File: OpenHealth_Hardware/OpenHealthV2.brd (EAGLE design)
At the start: 128.3 x 134.6 mm, 25 parts

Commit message: Reparacion de placa principal - modo demo
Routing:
- net GND: track 140.3 -> 0.00 mm
- net VIN: track 85.2 -> 0.00 mm
- net LCA_RED: track 79.8 -> 0.00 mm
- net LCA_BLK: track 72.2 -> 0.00 mm
- net LCA_WHT: track 64.6 -> 0.00 mm
- net D_SCL: track 63.2 -> 0.00 mm
- net D_SDA: track 62.1 -> 0.00 mm
- net D12: track 58.5 -> 0.00 mm
- net LCA_GRN: track 56.9 -> 0.00 mm
- net LCA_YLW: track 49.3 -> 0.00 mm
- net LCA_CLK: track 32.1 -> 0.00 mm
- net LCA_DAT: track 29.5 -> 0.00 mm
- net 3.3V: track 18.6 -> 0.00 mm
- net B2: track 11.1 -> 0.00 mm
- net B1: track 7.32 -> 0.00 mm
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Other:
- board size 128.3 x 134.6 mm -> 128.3 x 133.3 mm

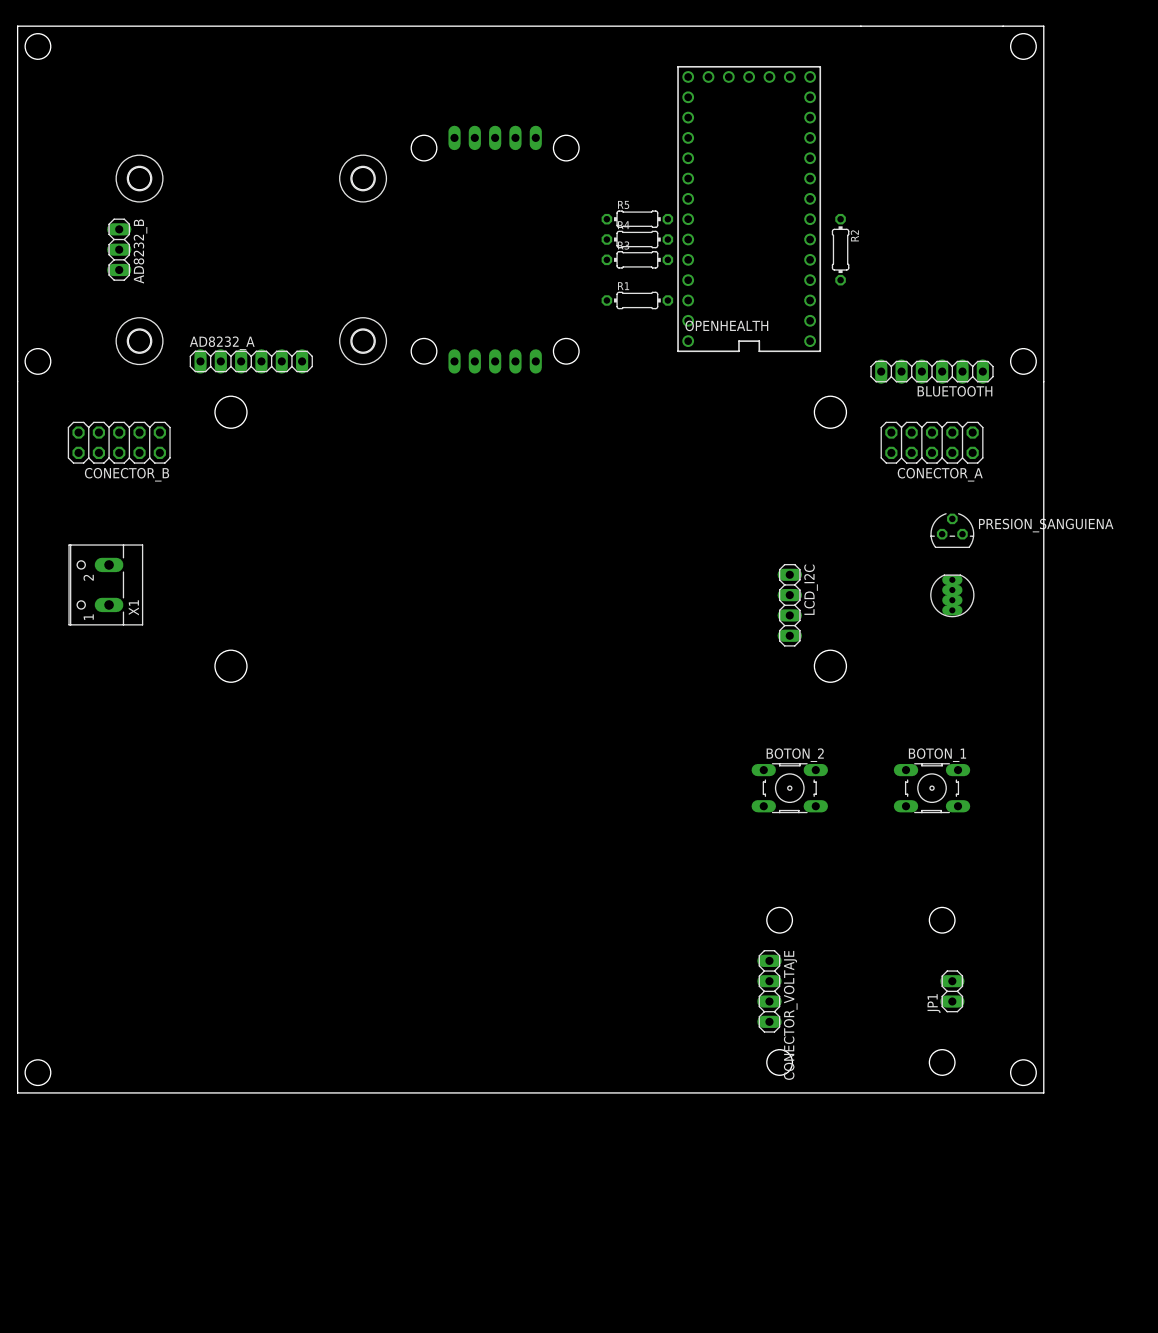
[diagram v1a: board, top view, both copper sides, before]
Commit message: Creacion de la Primera Libreria
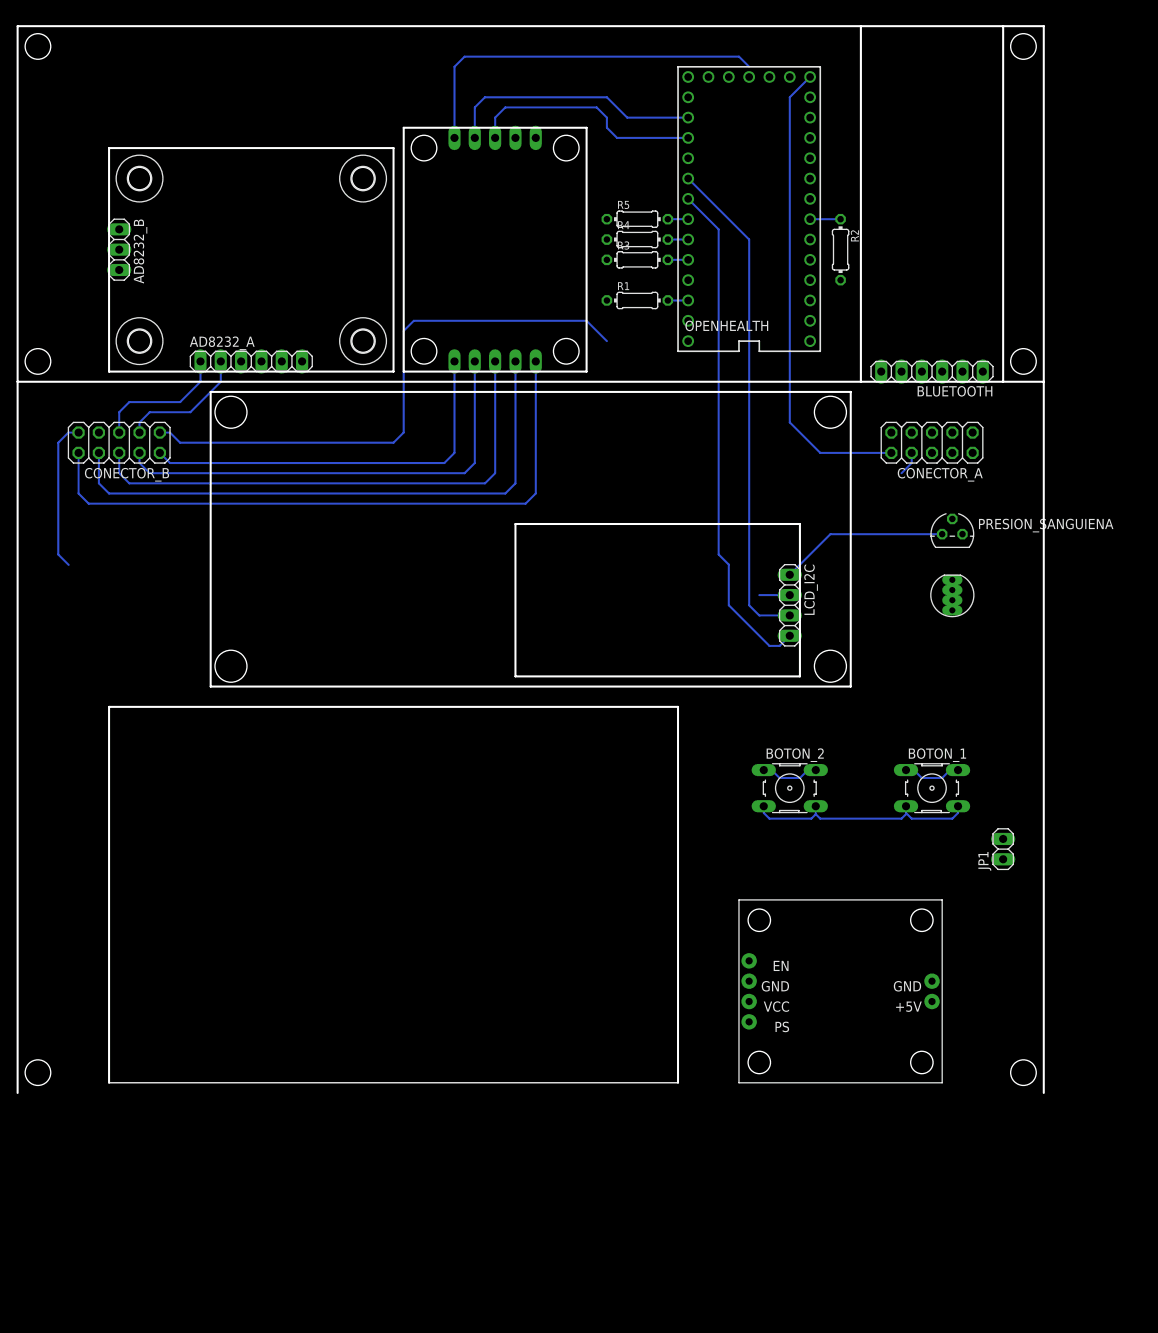
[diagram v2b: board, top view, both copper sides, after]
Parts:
- removed CONECTOR_VOLTAJE: (no value), pinhead:1X04
- removed X1: (no value), con-wago-500:W237-102
- added U$5: LIPOWER, Bateria:LIPOWER
- moved JP1 18.9 mm to (54.6, 50.8)
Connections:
- removed net N$1: CONECTOR_VOLTAJE.1, X1.1
- new net N$5: OPENHEALTH.VIN
- new net PIN_EN: JP1.1, U$5.PIN_EN
- net GND: now also JP1.2, U$5.PIN_GND1, U$5.PIN_GND2; no longer CONECTOR_VOLTAJE.2, X1.2
- net VIN: no longer CONECTOR_VOLTAJE.3, OPENHEALTH.VIN
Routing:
- net GND: track 0.00 -> 134.0 mm
- net LCA_RED: track 0.00 -> 79.8 mm
- net VIN: track 0.00 -> 75.0 mm
- net LCA_BLK: track 0.00 -> 72.2 mm
- net LCA_WHT: track 0.00 -> 64.6 mm
- net D_SCL: track 0.00 -> 63.2 mm
- net D_SDA: track 0.00 -> 62.1 mm
- net D12: track 0.00 -> 58.5 mm
- net LCA_GRN: track 0.00 -> 56.9 mm
- net LCA_YLW: track 0.00 -> 49.3 mm
- net LCA_CLK: track 0.00 -> 32.1 mm
- net LCA_DAT: track 0.00 -> 29.5 mm
- net 3.3V: track 0.00 -> 18.6 mm
- net B2: track 0.00 -> 11.1 mm
- net B1: track 0.00 -> 7.32 mm
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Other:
- outline, holes or cut-outs redrawn

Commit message: Creacion de los modulos de bluetooth y ad8232 asi como el cambio de nombre de la libreria y la utilizacion de la libreria en el proyecto
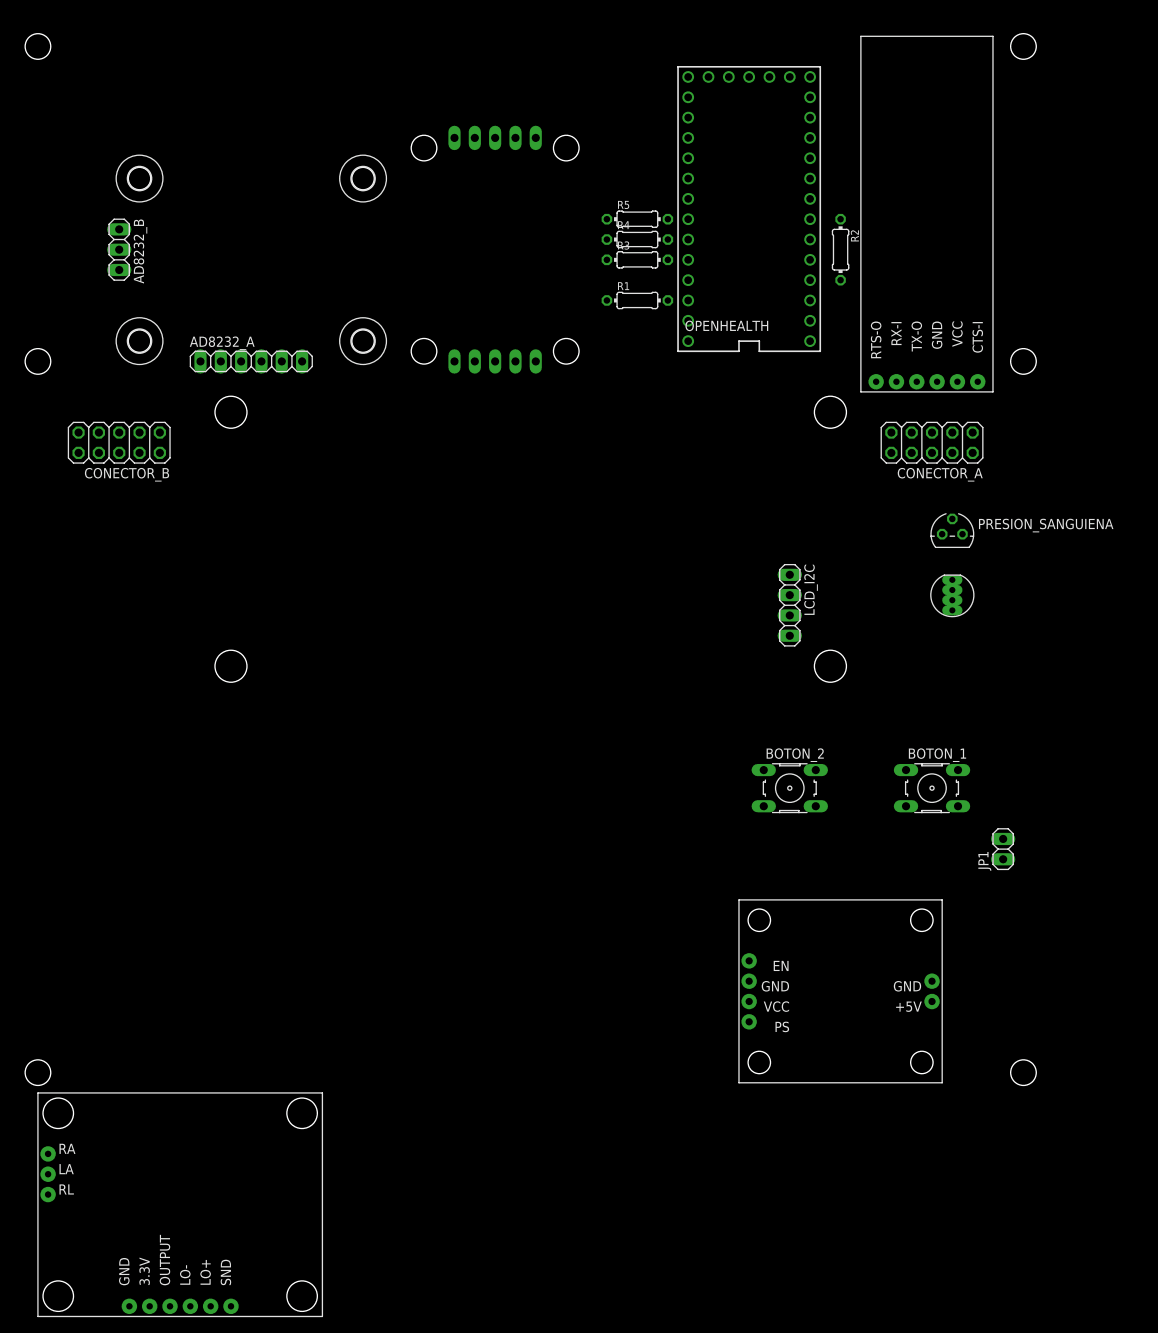
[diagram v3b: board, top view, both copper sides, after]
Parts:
- removed BLUETOOTH: (no value), pinhead:1X06
- added U$6: BLUETOOTH_HC05, OpenHealth:BLUETOOTH_HC05
- added U$7: AD8232, OpenHealth:AD8232
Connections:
- net BLUETOOTH_RX: now also U$6.PIN_RX-I; no longer BLUETOOTH.2
- net BLUETOOTH_TX: no longer BLUETOOTH.3
- net GND: now also U$6.PIN_GND; no longer BLUETOOTH.4
- net N$5: now also U$5.PIN_VCC
- net VIN: now also U$6.PIN_VCC; no longer BLUETOOTH.5
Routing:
- net GND: track 134.0 -> 0.00 mm
- net LCA_RED: track 79.8 -> 0.00 mm
- net VIN: track 75.0 -> 0.00 mm
- net LCA_BLK: track 72.2 -> 0.00 mm
- net LCA_WHT: track 64.6 -> 0.00 mm
- net D_SCL: track 63.2 -> 0.00 mm
- net D_SDA: track 62.1 -> 0.00 mm
- net D12: track 58.5 -> 0.00 mm
- net LCA_GRN: track 56.9 -> 0.00 mm
- net LCA_YLW: track 49.3 -> 0.00 mm
- net LCA_CLK: track 32.1 -> 0.00 mm
- net LCA_DAT: track 29.5 -> 0.00 mm
- net 3.3V: track 18.6 -> 0.00 mm
- net B2: track 11.1 -> 0.00 mm
- net B1: track 7.32 -> 0.00 mm
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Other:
- board outline removed

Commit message: Finalizacion de la primera version, listo para revision
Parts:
- removed AD8232_A: (no value), pinhead:1X06
- removed AD8232_B: (no value), pinhead:1X03
- removed LCA_SENSOR_PESO_A, LCA_SENSOR_PESO_B: (no value), pinhead:1X05
- removed LCD_I2C: (no value), pinhead:1X04
- removed U$4: (no value), holes:2,8
- added FRAME1: FRAME-LETTER, SparkFun-Aesthetics:CREATIVE_COMMONS
- added U$8: HX711, OpenHealth:HX711
- BOTON_1, BOTON_2, CONECTOR_A, CONECTOR_B, JP1: value (none) -> (none)
- U$1: value (none) -> I2C; device holes:2,8 -> OpenHealth:I2C
- U$2: value (none) -> BATERRY_MOLD; device holes:2,8 -> OpenHealth:BATTERY_MOLD
- U$3: device holes:2,8 -> SparkFun-Aesthetics:OSHW-LOGO-L
- moved U$7 157.5 mm to (-62.2, 149.9), turned to 270 degrees
- moved U$2 117.9 mm to (17.8, 20.3), turned to 90 degrees
- moved U$3 91.1 mm to (-61.0, 30.5)
- moved U$1 61.6 mm to (-44.5, 73.7)
- moved LED_RGB 56.7 mm to (1.27, 114.3), turned to 0 degrees
- moved PRESION_SANGUIENA 56.0 mm to (1.27, 120.7)
- moved JP1 39.4 mm to (54.6, 90.2)
- moved R2 36.4 mm to (1.27, 141.0), turned to 0 degrees
- moved U$6 34.3 mm to (10.2, 130.8), turned to 0 degrees
- moved R3 14.8 mm to (1.27, 137.2)
- moved R1 12.7 mm to (1.27, 129.5)
- moved OPENHEALTH 11.4 mm to (27.9, 120.7), turned to 90 degrees
- moved R4 9.92 mm to (1.27, 133.3)
- moved R5 8.52 mm to (1.27, 125.7)
- moved U$5 6.48 mm to (53.3, 20.3)
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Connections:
- removed net N$5: OPENHEALTH.VIN, U$5.PIN_VCC
- net 3.3V: now also U$7.PIN_3.3V; no longer AD8232_A.2
- net BLUETOOTH_TX: now also U$6.PIN_TX-O
- net D_SCL: now also U$1.SCL; no longer LCD_I2C.4
- net D_SDA: now also U$1.SDA; no longer LCD_I2C.3
- net GND: now also U$1.GND, U$7.PIN_GND, U$8.GND; no longer AD8232_A.1, LCA_SENSOR_PESO_A.5, LCD_I2C.1
- net LA: now also U$7.PIN_LA; no longer AD8232_B.2
- net LCA_BLK: now also U$8.BLK; no longer LCA_SENSOR_PESO_B.2
- net LCA_CLK: now also U$8.CLK; no longer LCA_SENSOR_PESO_A.4
- net LCA_DAT: now also U$8.DAT; no longer LCA_SENSOR_PESO_A.3
- net LCA_GRN: now also U$8.GRN; no longer LCA_SENSOR_PESO_B.4
- net LCA_RED: now also U$8.RED; no longer LCA_SENSOR_PESO_B.1
- net LCA_WHT: now also U$8.WHT; no longer LCA_SENSOR_PESO_B.3
- net LCA_YLW: now also U$8.YLW; no longer LCA_SENSOR_PESO_B.5
- net LO+: now also U$7.PIN_LO+; no longer AD8232_A.5
- net LO-: now also U$7.PIN_LO-; no longer AD8232_A.4
- net OUTPUT: now also U$7.PIN_OUTPUT; no longer AD8232_A.3
- net RA: now also U$7.PIN_RA; no longer AD8232_B.1
- net RL: now also U$7.PIN_RL; no longer AD8232_B.3
- net VIN: now also OPENHEALTH.VIN, U$1.VCC, U$5.PIN_VCC, U$8.VCC, U$8.VDD; no longer LCA_SENSOR_PESO_A.1, LCA_SENSOR_PESO_A.2, LCD_I2C.2
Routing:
- net N$6: track 0.00 -> 528.3 mm
- net GND: track 0.00 -> 345.2 mm
- net VIN: track 0.00 -> 300.7 mm
- net 3.3V: track 0.00 -> 164.8 mm, vias 0 -> 1
- net RL: track 0.00 -> 151.5 mm
- net LA: track 0.00 -> 130.4 mm, vias 0 -> 1
- net B1: track 0.00 -> 113.8 mm
- net RA: track 0.00 -> 110.1 mm, vias 0 -> 2
- net B2: track 0.00 -> 107.7 mm
- net OUTPUT: track 0.00 -> 97.4 mm, vias 0 -> 1
- net LO-: track 0.00 -> 92.7 mm, vias 0 -> 1
- net LO+: track 0.00 -> 92.4 mm, vias 0 -> 1
- net D_SDA: track 0.00 -> 87.2 mm, vias 0 -> 1
- net D_SCL: track 0.00 -> 85.6 mm, vias 0 -> 1
- net SALIDA_D6: track 0.00 -> 72.9 mm
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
